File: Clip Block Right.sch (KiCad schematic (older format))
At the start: 27 parts, among them J2 Conn_02x05_Odd_Even, SW17 B3F-5050, SW18 B3F-5050, SW19 B3F-5050, SW20 B3F-5050, SW21 B3F-5050, SW22 B3F-5050, SW23 B3F-5050, SW24 B3F-5050, SW25 B3F-5050, SW26 B3F-5050, SW27 B3F-5050, SW28 B3F-5050, SW29 B3F-5050, SW30 B3F-5050, SW31 B3F-5050, SW32 B3F-5050, U2 CD74HC4067M

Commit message: Housekeeping
Cleaned up the schematic for the subsidiary boards

Switched 5v and Com connections to make routing easier.
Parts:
- removed J2: Conn_02x05_Odd_Even, Connector_PinHeader_2.54mm:PinHeader_2x05_P2.54mm_Vertical, symbol Connector_Generic:Conn_02x05_Odd_Even
- added J2: Conn_02x05_Odd_Even, Connector_PinHeader_2.54mm:PinHeader_2x05_P2.54mm_Vertical, symbol Connector:Conn_01x10_Male
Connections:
- wire segments 183 -> 172
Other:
- moved on the sheet: SW_5, SW_6, SW_7, SW_8
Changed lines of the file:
@@
 Wire Wire Line
 	2700 950  2700 1150
-Wire Wire Line
-	2100 2550 2100 1750
 Connection ~ 2700 1150
 Wire Wire Line
 	2700 1150 2700 1250
-Wire Wire Line
-	2000 1150 2000 2650
 $Comp
 L cp_midi_control_surface_002-rescue:SW_SPST_4_PIN-sw_spst_0 SW?
@@
 Wire Wire Line
 	6400 5250 7300 5250
-Wire Wire Line
-	1900 2450 2200 2450
-Wire Wire Line
-	2100 1750 2200 1750
-Wire Wire Line
-	2000 1150 2700 1150
-Wire Wire Line
-	1850 2150 2200 2150
 $Comp
 L 74xx:CD74HC4067M U?
@@
 L cp_midi_control_surface_002-rescue:SW_SPST_4_PIN-sw_spst_0 SW?
 U 1 1 5D610099
-P 2150 4050
+P 2100 3800
 AR Path="/5C4B73B3/5D610099" Ref="SW?"  Part="1"
 AR Path="/5C4BA289/5D610099" Ref="SW?"  Part="1"
 AR Path="/5D610099" Ref="SW?"  Part="1"
 AR Path="/5C4B9DB9/5D610099" Ref="SW_5"  Part="1"
-F 0 "SW_5" H 2150 3850 50  0000 C CNN
-F 1 "B3F-5050" H 2150 4224 50  0001 C CNN
-F 2 "cunabulapress-footprints:Omron_B3F-5050" H 2150 4200 50  0001 C CNN
-F 3 "" H 2150 4200 50  0001 C CNN
-	1    2150 4050
+F 0 "SW_5" H 2100 3600 50  0000 C CNN
+F 1 "B3F-5050" H 2100 3974 50  0001 C CNN
+F 2 "cunabulapress-footprints:Omron_B3F-5050" H 2100 3950 50  0001 C CNN
+F 3 "" H 2100 3950 50  0001 C CNN
+	1    2100 3800
 	1    0    0    -1
 $EndComp
@@
 L cp_midi_control_surface_002-rescue:SW_SPST_4_PIN-sw_spst_0 SW?
 U 1 1 5D6100A0
-P 2150 4550
+P 2100 4300
 AR Path="/5C4B73B3/5D6100A0" Ref="SW?"  Part="1"
 AR Path="/5C4BA289/5D6100A0" Ref="SW?"  Part="1"
 AR Path="/5D6100A0" Ref="SW?"  Part="1"
 AR Path="/5C4B9DB9/5D6100A0" Ref="SW_6"  Part="1"
-F 0 "SW_6" H 2150 4350 50  0000 C CNN
-F 1 "B3F-5050" H 2150 4724 50  0001 C CNN
-F 2 "cunabulapress-footprints:Omron_B3F-5050" H 2150 4700 50  0001 C CNN
-F 3 "" H 2150 4700 50  0001 C CNN
-	1    2150 4550
+F 0 "SW_6" H 2100 4100 50  0000 C CNN
+F 1 "B3F-5050" H 2100 4474 50  0001 C CNN
+F 2 "cunabulapress-footprints:Omron_B3F-5050" H 2100 4450 50  0001 C CNN
+F 3 "" H 2100 4450 50  0001 C CNN
+	1    2100 4300
 	1    0    0    -1
 $EndComp
@@
 L cp_midi_control_surface_002-rescue:SW_SPST_4_PIN-sw_spst_0 SW?
 U 1 1 5D6100A7
-P 2150 5050
+P 2100 4800
 AR Path="/5C4B73B3/5D6100A7" Ref="SW?"  Part="1"
 AR Path="/5C4BA289/5D6100A7" Ref="SW?"  Part="1"
 AR Path="/5D6100A7" Ref="SW?"  Part="1"
 AR Path="/5C4B9DB9/5D6100A7" Ref="SW_7"  Part="1"
-F 0 "SW_7" H 2150 4850 50  0000 C CNN
-F 1 "B3F-5050" H 2150 5224 50  0001 C CNN
-F 2 "cunabulapress-footprints:Omron_B3F-5050" H 2150 5200 50  0001 C CNN
-F 3 "" H 2150 5200 50  0001 C CNN
-	1    2150 5050
+F 0 "SW_7" H 2100 4600 50  0000 C CNN
+F 1 "B3F-5050" H 2100 4974 50  0001 C CNN
+F 2 "cunabulapress-footprints:Omron_B3F-5050" H 2100 4950 50  0001 C CNN
+F 3 "" H 2100 4950 50  0001 C CNN
+	1    2100 4800
 	1    0    0    -1
 $EndComp
@@
 L cp_midi_control_surface_002-rescue:SW_SPST_4_PIN-sw_spst_0 SW?
 U 1 1 5D6100AE
-P 2150 5550
+P 2100 5300
 AR Path="/5C4B73B3/5D6100AE" Ref="SW?"  Part="1"
 AR Path="/5C4BA289/5D6100AE" Ref="SW?"  Part="1"
 AR Path="/5D6100AE" Ref="SW?"  Part="1"
 AR Path="/5C4B9DB9/5D6100AE" Ref="SW_8"  Part="1"
-F 0 "SW_8" H 2150 5350 50  0000 C CNN
-F 1 "B3F-5050" H 2150 5724 50  0001 C CNN
-F 2 "cunabulapress-footprints:Omron_B3F-5050" H 2150 5700 50  0001 C CNN
-F 3 "" H 2150 5700 50  0001 C CNN
-	1    2150 5550
-	1    0    0    -1
-$EndComp
-Wire Wire Line
-	2350 5550 2500 5550
-Wire Wire Line
-	2350 5050 2500 5050
-Connection ~ 2500 5050
-Wire Wire Line
-	2500 5050 2500 5550
-Wire Wire Line
-	2350 4550 2500 4550
-Connection ~ 2500 4550
-Wire Wire Line
-	2500 4550 2500 5050
-Wire Wire Line
-	2350 4050 2500 4050
-Wire Wire Line
-	2500 4050 2500 4550
-NoConn ~ 2350 4150
-NoConn ~ 2350 4650
-NoConn ~ 2350 5150
-NoConn ~ 1950 5650
-NoConn ~ 2350 5650
-Connection ~ 2500 5550
-Wire Wire Line
-	2500 5550 2500 6100
-Wire Wire Line
-	2700 6100 2500 6100
-$Comp
-L Connector_Generic:Conn_02x05_Odd_Even J2
-U 1 1 5D61E5D0
-P 1250 2350
-F 0 "J2" H 1300 2767 50  0000 C CNN
-F 1 "Conn_02x05_Odd_Even" H 1300 2676 50  0000 C CNN
-F 2 "Connector_PinHeader_2.54mm:PinHeader_2x05_P2.54mm_Vertical" H 1250 2350 50  0001 C CNN
-F 3 "~" H 1250 2350 50  0001 C CNN
-	1    1250 2350
-	1    0    0    -1
-$EndComp
-Wire Wire Line
-	1850 2150 1850 1650
-Wire Wire Line
-	1850 1650 750  1650
-Wire Wire Line
-	750  1650 750  2150
-Wire Wire Line
-	750  2150 1050 2150
-Wire Wire Line
-	1800 2250 1800 2150
-Wire Wire Line
-	1800 2150 1550 2150
-Wire Wire Line
-	1800 2250 2200 2250
-Wire Wire Line
-	1750 2350 1750 2250
-Wire Wire Line
-	1750 2250 1550 2250
-Wire Wire Line
-	1750 2350 2200 2350
-Wire Wire Line
-	1900 2450 1900 1400
-Wire Wire Line
-	1900 1400 650  1400
-Wire Wire Line
-	650  2250 1050 2250
-Wire Wire Line
-	650  1400 650  2250
-Wire Wire Line
-	1700 2550 1700 2350
-Wire Wire Line
-	1700 2350 1550 2350
-Wire Wire Line
-	1700 2550 2100 2550
-Wire Wire Line
-	850  2650 850  2350
-Wire Wire Line
-	850  2350 1050 2350
-Wire Wire Line
-	850  2650 2000 2650
+F 0 "SW_8" H 2100 5100 50  0000 C CNN
+F 1 "B3F-5050" H 2100 5474 50  0001 C CNN
+F 2 "cunabulapress-footprints:Omron_B3F-5050" H 2100 5450 50  0001 C CNN
+F 3 "" H 2100 5450 50  0001 C CNN
+	1    2100 5300
+	1    0    0    -1
+$EndComp
+Wire Wire Line
+	2300 5300 2450 5300
+Wire Wire Line
+	2300 4800 2450 4800
+Connection ~ 2450 4800
+Wire Wire Line
+	2450 4800 2450 5300
+Wire Wire Line
+	2300 4300 2450 4300
+Connection ~ 2450 4300
+Wire Wire Line
+	2450 4300 2450 4800
+Wire Wire Line
+	2300 3800 2450 3800
+Wire Wire Line
+	2450 3800 2450 4300
+NoConn ~ 2300 3900
+NoConn ~ 2300 4400
+NoConn ~ 2300 4900
+NoConn ~ 1900 5400
+NoConn ~ 2300 5400
+Connection ~ 2450 5300
 $Comp
 L power:GND #PWR?
@@
 NoConn ~ 750  6950
 NoConn ~ 750  7050
-Wire Wire Line
-	1950 4150 1850 4150
-Wire Wire Line
-	1850 4150 1850 2450
-Wire Wire Line
-	1850 2450 1550 2450
-Wire Wire Line
-	1950 4650 1600 4650
-Wire Wire Line
-	1600 4650 1600 2550
-Wire Wire Line
-	1600 2550 1550 2550
-Wire Wire Line
-	1950 5150 1050 5150
-Wire Wire Line
-	1050 5150 1050 2550
-Wire Wire Line
-	1050 2450 950  2450
-Wire Wire Line
-	950  2450 950  5550
-Wire Wire Line
-	950  5550 1950 5550
-NoConn ~ 1950 4050
-NoConn ~ 1950 4550
-NoConn ~ 1950 5050
+NoConn ~ 1900 3800
+NoConn ~ 1900 4300
+NoConn ~ 1900 4800
+$Comp
+L Connector:Conn_01x10_Male J?
+U 1 1 5D71A9DE
+P 750 2550
+AR Path="/5C4B73B3/5D71A9DE" Ref="J?"  Part="1"
+AR Path="/5C4B9DB9/5D71A9DE" Ref="J2"  Part="1"
+F 0 "J2" H 750 3100 50  0000 C CNN
+F 1 "Conn_02x05_Odd_Even" H 800 2876 50  0001 C CNN
+F 2 "Connector_PinHeader_2.54mm:PinHeader_2x05_P2.54mm_Vertical" H 750 2550 50  0001 C CNN
+F 3 "~" H 750 2550 50  0001 C CNN
+	1    750  2550
+	1    0    0    -1
+$EndComp
+Wire Wire Line
+	1900 4400 1800 4400
+Wire Wire Line
+	1900 4900 1700 4900
+Wire Wire Line
+	1900 5300 1500 5300
+Wire Wire Line
+	2200 2150 950  2150
+Wire Wire Line
+	950  2250 2200 2250
+Wire Wire Line
+	950  2550 1700 2550
+Wire Wire Line
+	1700 2550 1700 1750
+Wire Wire Line
+	950  2650 1500 2650
+Wire Wire Line
+	1500 2650 1500 1150
+Wire Wire Line
+	1900 2450 950  2450
+Wire Wire Line
+	950  2350 1900 2350
+Wire Wire Line
+	950  2750 1500 2750
+Wire Wire Line
+	1500 2750 1500 5300
+Wire Wire Line
+	950  2850 1600 2850
+Wire Wire Line
+	1600 2850 1600 3900
+Wire Wire Line
+	1600 3900 1900 3900
+Wire Wire Line
+	950  2950 1700 2950
+Wire Wire Line
+	1700 2950 1700 4900
+Wire Wire Line
+	950  3050 1800 3050
+Wire Wire Line
+	1800 3050 1800 4400
+Wire Wire Line
+	1700 1750 2200 1750
+Wire Wire Line
+	2450 5300 2450 6100
+Wire Wire Line
+	2450 6100 2700 6100
+Wire Wire Line
+	2200 2350 2100 2350
+Wire Wire Line
+	2100 2450 2200 2450
+Wire Wire Line
+	1900 2350 2100 2450
+Wire Wire Line
+	2100 2350 1900 2450
+Wire Wire Line
+	1500 1150 2700 1150
 $EndSCHEMATC

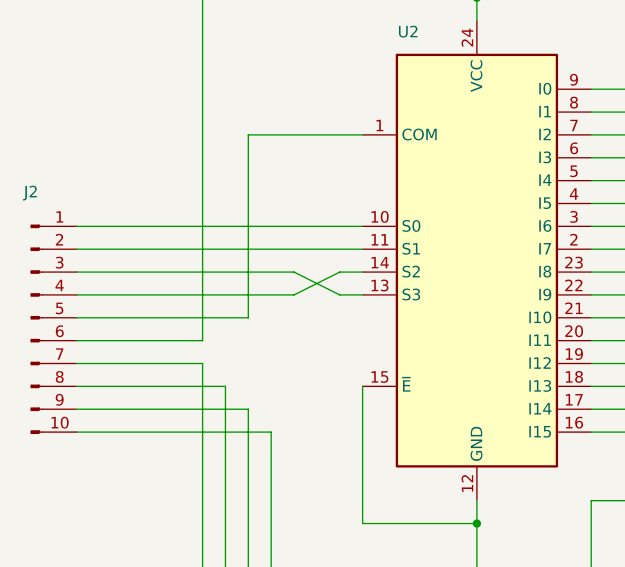
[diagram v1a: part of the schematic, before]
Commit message: Fixed S0-S3 Rail, added LEDS
Was an error on the schematic, easily fixed without changing the traces, glad I left it before deleting them all.

LEDs and relate resistors are in.
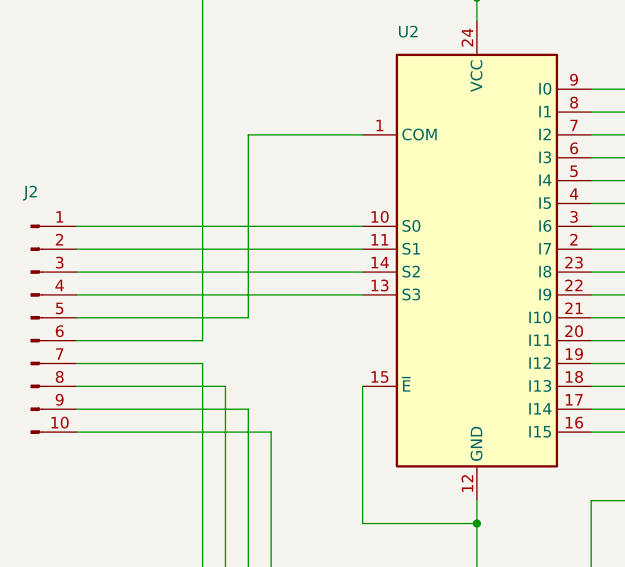
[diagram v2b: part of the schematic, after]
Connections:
- net at U2.13 (S3): now also J2.4 (Pin_4); no longer J2.3 (Pin_3)
- net at U2.14 (S2): now also J2.3 (Pin_3); no longer J2.4 (Pin_4)
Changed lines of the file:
@@
 	1500 2650 1500 1150
-Wire Wire Line
-	1900 2450 950  2450
-Wire Wire Line
-	950  2350 1900 2350
 Wire Wire Line
 	950  2750 1500 2750
@@
 	2450 6100 2700 6100
 Wire Wire Line
-	2200 2350 2100 2350
+	1500 1150 2700 1150
 Wire Wire Line
-	2100 2450 2200 2450
+	950  2350 2200 2350
 Wire Wire Line
-	1900 2350 2100 2450
-Wire Wire Line
-	2100 2350 1900 2450
-Wire Wire Line
-	1500 1150 2700 1150
+	950  2450 2200 2450
 $EndSCHEMATC

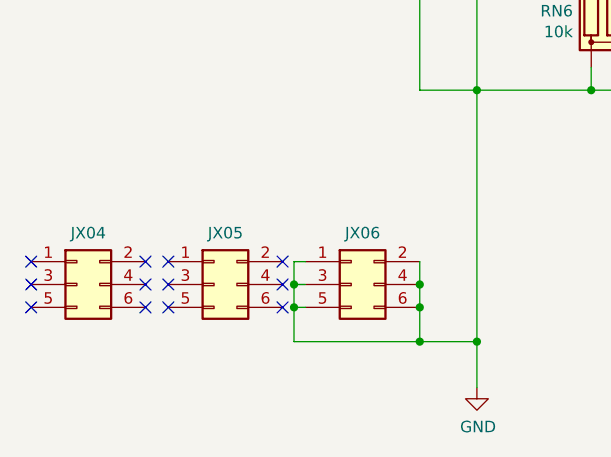
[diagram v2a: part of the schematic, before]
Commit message: Rails done, GND corrected.
Now for checking and decals
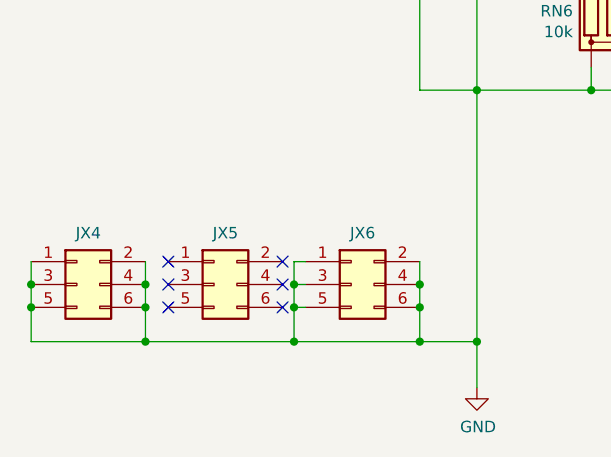
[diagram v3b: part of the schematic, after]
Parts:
- renumbered JX04 to JX4, JX05 to JX5, JX06 to JX6
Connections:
- net GND: now also JX4.1 (Pin_1), JX4.2 (Pin_2), JX4.3 (Pin_3), JX4.4 (Pin_4), JX4.5 (Pin_5), JX4.6 (Pin_6)
- no-connect marks 52 -> 46
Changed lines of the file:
@@
 $Descr A4 11693 8268
 encoding utf-8
-Sheet 7 8
+Sheet 7 9
 Title ""
 Date ""
@@
 P 950 6950
 AR Path="/5C4B73B3/5D8DA342" Ref="JX?"  Part="1"
-AR Path="/5C4B9DB9/5D8DA342" Ref="JX04"  Part="1"
-F 0 "JX04" H 1000 7175 50  0000 C CNN
+AR Path="/5C4B9DB9/5D8DA342" Ref="JX4"  Part="1"
+F 0 "JX4" H 1000 7175 50  0000 C CNN
 F 1 "Conn_02x03_Odd_Even" H 1000 7176 50  0001 C CNN
 F 2 "Connector_PinHeader_2.54mm:PinHeader_2x03_P2.54mm_Vertical" H 950 6950 50  0001 C CNN
@@
 P 2150 6950
 AR Path="/5C4B73B3/5D8DA349" Ref="JX?"  Part="1"
-AR Path="/5C4B9DB9/5D8DA349" Ref="JX06"  Part="1"
-F 0 "JX06" H 2200 7175 50  0000 C CNN
+AR Path="/5C4B9DB9/5D8DA349" Ref="JX6"  Part="1"
+F 0 "JX6" H 2200 7175 50  0000 C CNN
 F 1 "Conn_02x03_Odd_Even" H 2200 7176 50  0001 C CNN
 F 2 "Connector_PinHeader_2.54mm:PinHeader_2x03_P2.54mm_Vertical" H 2150 6950 50  0001 C CNN
@@
 P 1550 6950
 AR Path="/5C4B73B3/5D8DA359" Ref="JX?"  Part="1"
-AR Path="/5C4B9DB9/5D8DA359" Ref="JX05"  Part="1"
-F 0 "JX05" H 1600 7175 50  0000 C CNN
+AR Path="/5C4B9DB9/5D8DA359" Ref="JX5"  Part="1"
+F 0 "JX5" H 1600 7175 50  0000 C CNN
 F 1 "Conn_02x03_Odd_Even" H 1600 7176 50  0001 C CNN
 F 2 "Connector_PinHeader_2.54mm:PinHeader_2x03_P2.54mm_Vertical" H 1550 6950 50  0001 C CNN
@@
 NoConn ~ 1350 6950
 NoConn ~ 1350 6850
-NoConn ~ 1250 6850
-NoConn ~ 1250 6950
-NoConn ~ 1250 7050
-NoConn ~ 750  6850
-NoConn ~ 750  6950
-NoConn ~ 750  7050
 NoConn ~ 1900 3800
 NoConn ~ 1900 4300
@@
 Wire Wire Line
 	950  2450 2200 2450
+Wire Wire Line
+	1250 6850 1250 6950
+Connection ~ 1250 6950
+Wire Wire Line
+	1250 6950 1250 7050
+Connection ~ 1250 7050
+Wire Wire Line
+	1250 7050 1250 7200
+Connection ~ 1900 7200
+Wire Wire Line
+	750  6850 750  6950
+Wire Wire Line
+	750  7200 1250 7200
+Connection ~ 750  6950
+Wire Wire Line
+	750  6950 750  7050
+Connection ~ 750  7050
+Wire Wire Line
+	750  7050 750  7200
+Connection ~ 1250 7200
+Wire Wire Line
+	1250 7200 1900 7200
 $EndSCHEMATC
